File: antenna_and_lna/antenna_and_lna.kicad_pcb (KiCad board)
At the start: 2 copper layers, 9 parts, among them Q1 2SK3557

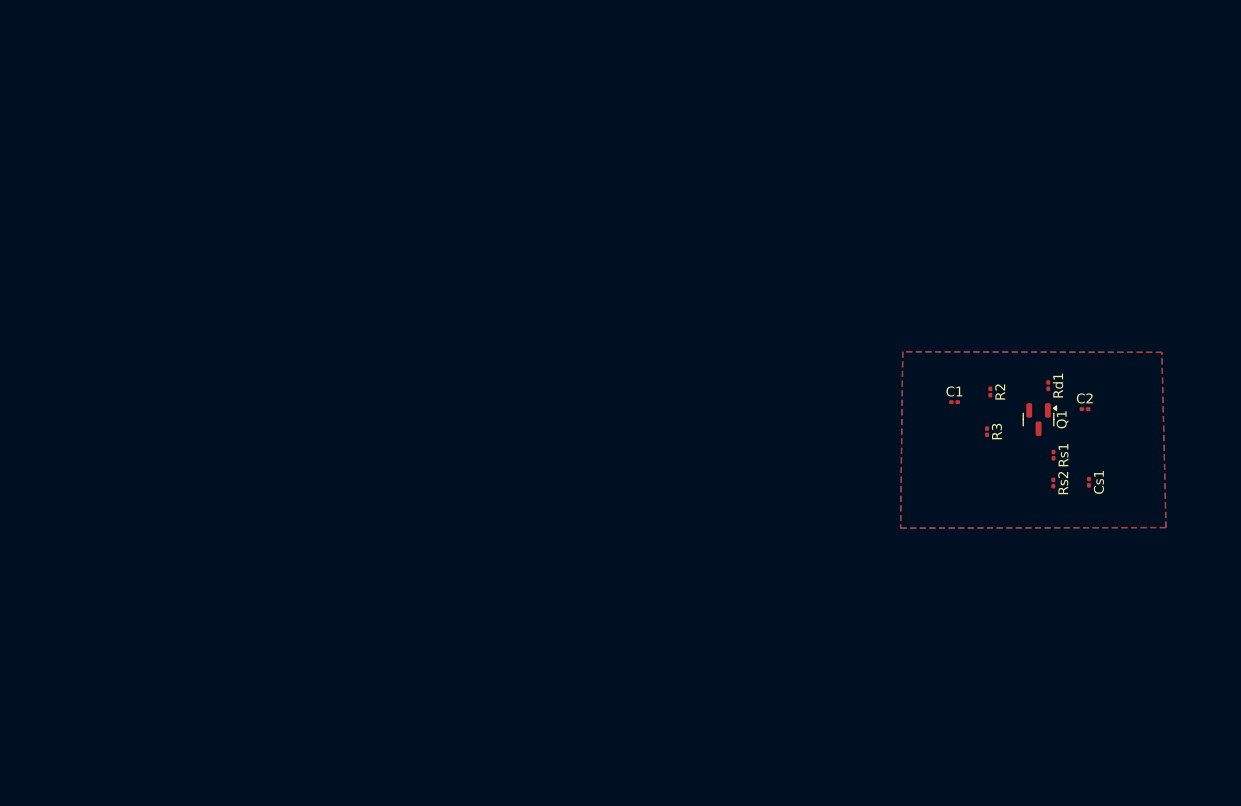
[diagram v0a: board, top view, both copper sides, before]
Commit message: add really rough and imprecise (not to scale at all!) footprints for antenna and tuning cap array
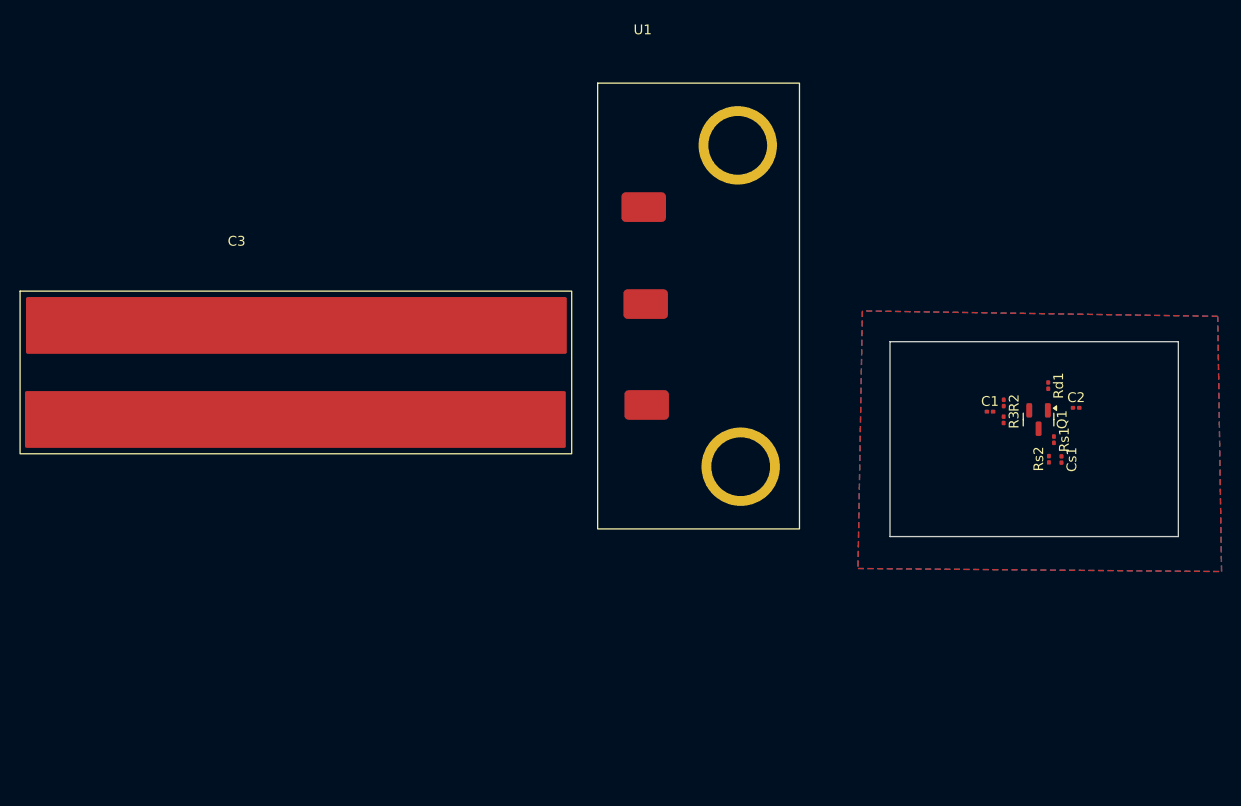
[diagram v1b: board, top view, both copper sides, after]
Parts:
- added C3: C, custom:Tuning_Cap, F.Cu at (77.1, 72.1)
- added U1: ~, custom:Antenna, F.Cu at (118.6, 50.5)
- moved C1 3.74 mm to (154.0, 89.0)
- moved Cs1 3.64 mm to (161.3, 93.9)
- moved Rs2 2.47 mm to (160.1, 93.8)
- moved R3 2.09 mm to (155.4, 89.8)
- moved R2 1.77 mm to (155.4, 88.1)
- moved Rs1 1.58 mm to (160.6, 91.8)
- moved C2 0.92 mm to (162.8, 88.6)
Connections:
- C1 pad 1: unconnected-(C1-Pad1) -> /LNA_in
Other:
- board outline added: 29.4 x 19.9 mm
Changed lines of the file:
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@@
 	(net 2 "Net-(Q1-S)")
 	(net 3 "/LNA/Sigout")
-	(net 4 "unconnected-(C1-Pad1)")
+	(net 4 "/LNA_in")
 	(net 5 "unconnected-(C2-Pad2)")
 	(net 6 "Net-(Cs1-Pad1)")
 	(net 7 "GND")
 	(net 8 "+5V")
+	(net 9 "Net-(U1-Tune)")
 	(footprint "Resistor_SMD:R_0201_0603Metric"
 		(layer "F.Cu")
@@
 	(footprint "Resistor_SMD:R_0201_0603Metric"
 		(layer "F.Cu")
-		(at 154.07 86.975 -90)
+		(at 155.44 88.095 -90)
 		(descr "Resistor SMD 0201 (0603 Metric), square (rectangular) end terminal, IPC-7351 nominal, (Body size source: https://www.vishay.com/docs/20052/crcw0201e3.pdf), generated with kicad-footprint-generator")
 		(tags "resistor")
@@
 	(footprint "Capacitor_SMD:C_0201_0603Metric"
 		(layer "F.Cu")
-		(at 164.14 96.18 -90)
+		(at 161.33 93.865 -90)
 		(descr "Capacitor SMD 0201 (0603 Metric), square (rectangular) end terminal, IPC-7351 nominal, (Body size source: https://www.vishay.com/docs/20052/crcw0201e3.pdf), generated with kicad-footprint-generator")
 		(tags "capacitor")
@@
 	(footprint "Resistor_SMD:R_0201_0603Metric"
 		(layer "F.Cu")
-		(at 160.5 96.27 -90)
+		(at 160.05 93.84 -90)
 		(descr "Resistor SMD 0201 (0603 Metric), square (rectangular) end terminal, IPC-7351 nominal, (Body size source: https://www.vishay.com/docs/20052/crcw0201e3.pdf), generated with kicad-footprint-generator")
 		(tags "resistor")
 		(property "Reference" "Rs2"
-			(at 0 -1.05 90)
+			(at -0.035 1.05 90)
 			(layer "F.SilkS")
 			(effects
@@
 		)
 	)
+	(footprint "custom:Tuning_Cap"
+		(layer "F.Cu")
+		(at 77.14 72.08)
+		(property "Reference" "C3"
+			(at 0 -0.5 0)
+			(unlocked yes)
+			(layer "F.SilkS")
+			(effects
+				(font
+					(size 1 1)
+					(thickness 0.1)
+				)
+			)
+		)
+		(property "Value" "C"
+			(at 0 1 0)
+			(unlocked yes)
+			(layer "F.Fab")
+			(effects
+				(font
+					(size 1 1)
+					(thickness 0.15)
+				)
+			)
+		)
+		(property "Datasheet" "~"
+			(at 0 0 0)
+			(unlocked yes)
+			(layer "F.Fab")
+			(hide yes)
+			(effects
+				(font
+					(size 1 1)
+					(thickness 0.15)
+				)
+			)
+		)
+		(property "Description" "Unpolarized capacitor"
+			(at 0 0 0)
+			(unlocked yes)
+			(layer "F.Fab")
+			(hide yes)
+			(effects
+				(font
+					(size 1 1)
+					(thickness 0.15)
+				)
+			)
+		)
+		(property ki_fp_filters "C_*")
+		(sheetname "/")
+		(sheetfile "antenna_and_lna.kicad_sch")
+		(attr smd)
+		(fp_rect
+			(start -22.1 4.6)
+			(end 34.2 21.2)
+			(stroke
+				(width 0.1)
+				(type default)
+			)
+			(fill no)
+			(layer "F.SilkS")
+		)
+		(fp_text user "${REFERENCE}"
+			(at 0 2.5 0)
+			(unlocked yes)
+			(layer "F.Fab")
+			(effects
+				(font
+					(size 1 1)
+					(thickness 0.15)
+				)
+			)
+		)
+		(pad "1" smd roundrect
+			(at 6.1 8.1)
+			(size 55.2 5.8)
+			(layers "F.Cu" "F.Mask" "F.Paste")
+			(roundrect_rratio 0.03125)
+			(net 7 "GND")
+			(pintype "passive")
+		)
+		(pad "2" smd roundrect
+			(at 6 17.7)
+			(size 55.2 5.8)
+			(layers "F.Cu" "F.Mask" "F.Paste")
+			(roundrect_rratio 0.03125)
+			(net 9 "Net-(U1-Tune)")
+			(pintype "passive")
+		)
+		(embedded_fonts no)
+	)
 	(footprint "Resistor_SMD:R_0201_0603Metric"
 		(layer "F.Cu")
-		(at 160.52 93.42 -90)
+		(at 160.56 91.845 -90)
 		(descr "Resistor SMD 0201 (0603 Metric), square (rectangular) end terminal, IPC-7351 nominal, (Body size source: https://www.vishay.com/docs/20052/crcw0201e3.pdf), generated with kicad-footprint-generator")
 		(tags "resistor")
@@
 	(footprint "Capacitor_SMD:C_0201_0603Metric"
 		(layer "F.Cu")
-		(at 150.425 88.01)
+		(at 154.035 88.98)
 		(descr "Capacitor SMD 0201 (0603 Metric), square (rectangular) end terminal, IPC-7351 nominal, (Body size source: https://www.vishay.com/docs/20052/crcw0201e3.pdf), generated with kicad-footprint-generator")
 		(tags "capacitor")
@@
 			(layers "F.Cu" "F.Mask")
 			(roundrect_rratio 0.25)
-			(net 4 "unconnected-(C1-Pad1)")
+			(net 4 "/LNA_in")
 			(pintype "passive")
 		)
@@
 	(footprint "Capacitor_SMD:C_0201_0603Metric"
 		(layer "F.Cu")
-		(at 163.735 88.72)
+		(at 162.825 88.59)
 		(descr "Capacitor SMD 0201 (0603 Metric), square (rectangular) end terminal, IPC-7351 nominal, (Body size source: https://www.vishay.com/docs/20052/crcw0201e3.pdf), generated with kicad-footprint-generator")
 		(tags "capacitor")
@@
 	(footprint "Resistor_SMD:R_0201_0603Metric"
 		(layer "F.Cu")
-		(at 153.73 91.025 -90)
+		(at 155.43 89.815 -90)
 		(descr "Resistor SMD 0201 (0603 Metric), square (rectangular) end terminal, IPC-7351 nominal, (Body size source: https://www.vishay.com/docs/20052/crcw0201e3.pdf), generated with kicad-footprint-generator")
 		(tags "resistor")
@@
 			)
 		)
+	)
+	(footprint "custom:Antenna"
+		(layer "F.Cu")
+		(at 118.59 50.5)
+		(property "Reference" "U1"
+			(at 0 -0.5 0)
+			(unlocked yes)
+			(layer "F.SilkS")
+			(effects
+				(font
+					(size 1 1)
+					(thickness 0.1)
+				)
+			)
+		)
+		(property "Value" "~"
+			(at 0 1 0)
+			(unlocked yes)
+			(layer "F.Fab")
+			(effects
+				(font
+					(size 1 1)
+					(thickness 0.15)
+				)
+			)
+		)
+		(property "Datasheet" ""
+			(at 0 0 0)
+			(unlocked yes)
+			(layer "F.Fab")
+			(hide yes)
+			(effects
+				(font
+					(size 1 1)
+					(thickness 0.15)
+				)
+			)
+		)
+		(property "Description" ""
+			(at 0 0 0)
+			(unlocked yes)
+			(layer "F.Fab")
+			(hide yes)
+			(effects
+				(font
+					(size 1 1)
+					(thickness 0.15)
+				)
+			)
+		)
+		(sheetname "/")
+		(sheetfile "antenna_and_lna.kicad_sch")
+		(attr smd)
+		(fp_rect
+			(start -4.6 4.95)
+			(end 16 50.45)
+			(stroke
+				(width 0.1)
+				(type default)
+			)
+			(fill no)
+			(layer "F.SilkS")
+		)
+		(fp_text user "${REFERENCE}"
+			(at 0 2.5 0)
+			(unlocked yes)
+			(layer "F.Fab")
+			(effects
+				(font
+					(size 1 1)
+					(thickness 0.15)
+				)
+			)
+		)
+		(pad "" np_thru_hole circle
+			(at 9.7 11.3)
+			(size 8 8)
+			(drill 6)
+			(layers "*.Cu" "*.Mask")
+		)
+		(pad "" np_thru_hole circle
+			(at 10 44.1)
+			(size 8 8)
+			(drill 6)
+			(layers "*.Cu" "*.Mask")
+		)
+		(pad "1" smd roundrect
+			(at 0.1 17.6)
+			(size 4.5525 3.035)
+			(layers "F.Cu" "F.Mask" "F.Paste")
+			(roundrect_rratio 0.15)
+			(net 4 "/LNA_in")
+			(pinfunction "Signal")
+			(pintype "bidirectional")
+		)
+		(pad "2" smd roundrect
+			(at 0.3 27.5)
+			(size 4.5525 3.035)
+			(layers "F.Cu" "F.Mask" "F.Paste")
+			(roundrect_rratio 0.15)
+			(net 7 "GND")
+			(pinfunction "Center_Tap")
+			(pintype "bidirectional")
+		)
+		(pad "3" smd roundrect
+			(at 0.4 37.8)
+			(size 4.5525 3.035)
+			(layers "F.Cu" "F.Mask" "F.Paste")
+			(roundrect_rratio 0.15)
+			(net 9 "Net-(U1-Tune)")
+			(pinfunction "Tune")
+			(pintype "bidirectional")
+		)
+		(embedded_fonts no)
+	)
+	(gr_rect
+		(start 143.83 81.84)
+		(end 173.26 101.73)
+		(stroke
+			(width 0.05)
+			(type default)
+		)
+		(fill no)
+		(layer "Edge.Cuts")
 	)
 	(zone
@@
 		(polygon
 			(pts
-				(xy 145.13 82.87) (xy 144.91 100.87) (xy 172 100.81) (xy 171.58 82.93)
-			)
-		)
+				(xy 141.01 78.7) (xy 140.56 104.99) (xy 177.67 105.3) (xy 177.28 79.25)
+			)
+		)

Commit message: update footprints for antenna and tuning caps
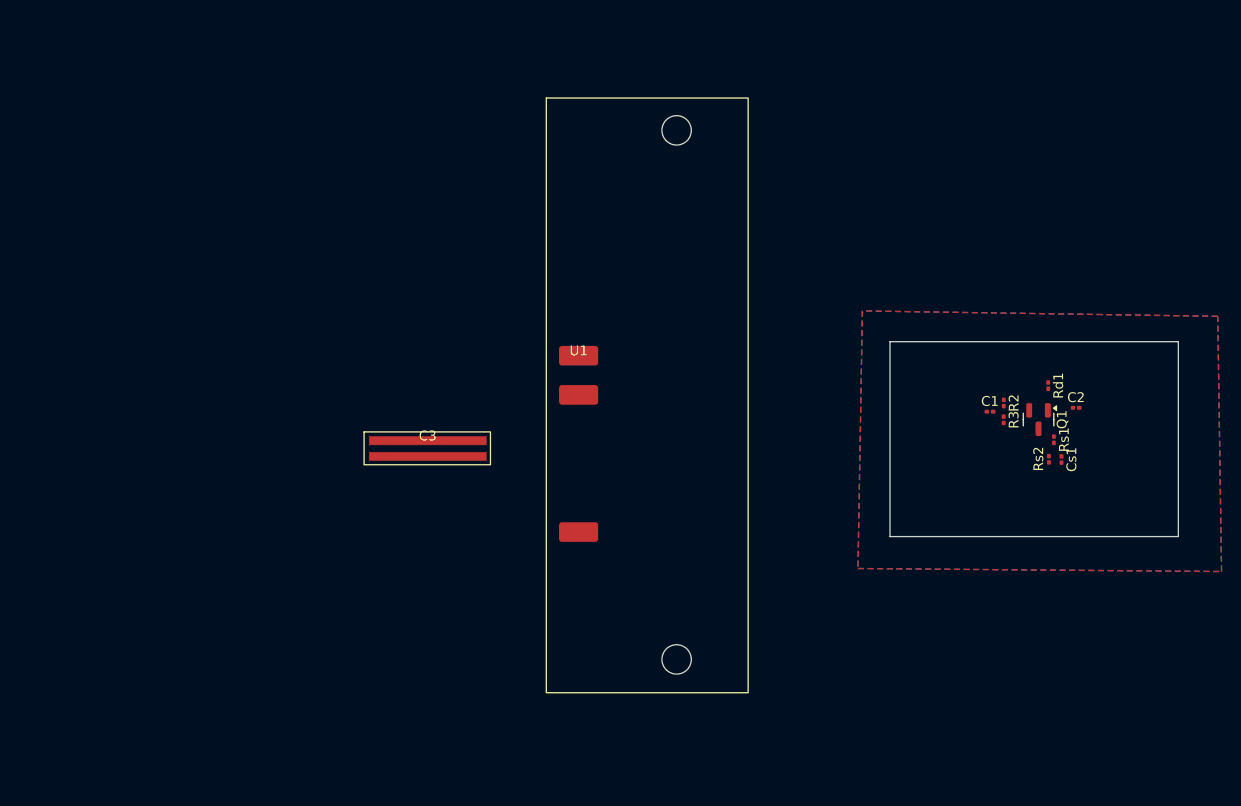
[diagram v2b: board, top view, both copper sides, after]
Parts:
- moved U1 33.4 mm to (112.0, 83.3)
- moved C3 27.8 mm to (96.7, 92.0)
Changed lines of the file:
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@@
 	(footprint "custom:Tuning_Cap"
 		(layer "F.Cu")
-		(at 77.14 72.08)
+		(at 96.65 91.95)
 		(property "Reference" "C3"
 			(at 0 -0.5 0)
@@
 		(attr smd)
 		(fp_rect
-			(start -22.1 4.6)
-			(end 34.2 21.2)
+			(start -6.5 -0.9)
+			(end 6.4 2.45)
 			(stroke
 				(width 0.1)
@@
 		)
 		(pad "1" smd roundrect
-			(at 6.1 8.1)
-			(size 55.2 5.8)
+			(at 0 0)
+			(size 12 0.9)
 			(layers "F.Cu" "F.Mask" "F.Paste")
 			(roundrect_rratio 0.03125)
@@
 		)
 		(pad "2" smd roundrect
-			(at 6 17.7)
-			(size 55.2 5.8)
+			(at 0 1.6)
+			(size 12 0.9)
 			(layers "F.Cu" "F.Mask" "F.Paste")
 			(roundrect_rratio 0.03125)
@@
 	(footprint "custom:Antenna"
 		(layer "F.Cu")
-		(at 118.59 50.5)
+		(at 112.05 83.27)
 		(property "Reference" "U1"
 			(at 0 -0.5 0)
@@
 		(attr smd)
 		(fp_rect
-			(start -4.6 4.95)
-			(end 16 50.45)
+			(start -3.3 -26.3)
+			(end 17.3 34.4)
 			(stroke
 				(width 0.1)
@@
 		)
 		(pad "" np_thru_hole circle
-			(at 9.7 11.3)
-			(size 8 8)
-			(drill 6)
+			(at 10 -23)
+			(size 3 3)
+			(drill 3)
 			(layers "*.Cu" "*.Mask")
 		)
 		(pad "" np_thru_hole circle
-			(at 10 44.1)
-			(size 8 8)
-			(drill 6)
+			(at 10 31)
+			(size 3 3)
+			(drill 3)
 			(layers "*.Cu" "*.Mask")
 		)
 		(pad "1" smd roundrect
-			(at 0.1 17.6)
-			(size 4.5525 3.035)
+			(at 0 0)
+			(size 4 2)
 			(layers "F.Cu" "F.Mask" "F.Paste")
 			(roundrect_rratio 0.15)
@@
 		)
 		(pad "2" smd roundrect
-			(at 0.3 27.5)
-			(size 4.5525 3.035)
+			(at 0 4)
+			(size 4 2)
 			(layers "F.Cu" "F.Mask" "F.Paste")
 			(roundrect_rratio 0.15)
@@
 		)
 		(pad "3" smd roundrect
-			(at 0.4 37.8)
-			(size 4.5525 3.035)
+			(at 0 18)
+			(size 4 2)
 			(layers "F.Cu" "F.Mask" "F.Paste")
 			(roundrect_rratio 0.15)

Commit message: main board gerbers and antenna board layout.
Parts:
- added C4: 10u, Capacitor_SMD:C_0603_1608Metric, F.Cu at (107.5, 83.3)
- added C5: 100n, Capacitor_SMD:C_0603_1608Metric, F.Cu at (98.7, 80.5)
- added C6: 3.3n, Capacitor_SMD:C_0603_1608Metric, F.Cu at (105.2, 104.4)
- added J1: CON-SMA-EDGE-S, SMA_fp:RFSOLUTIONS_CON-SMA-EDGE-S, F.Cu at (110.0, 124.3)
- added J2: TSW-104-14-F-S, pin_header_fp:CON4_1X4_TU_TSW, F.Cu at (112.5, 86.5)
- added L1: 27 u, Inductor_SMD:L_0603_1608Metric, F.Cu at (109.8, 117.6)
- C1: value C -> 100n; footprint Capacitor_SMD:C_0201_0603Metric -> Capacitor_SMD:C_0603_1608Metric
- C2: value C -> .012u; footprint Capacitor_SMD:C_0201_0603Metric -> Capacitor_SMD:C_0603_1608Metric
- Cs1: footprint Capacitor_SMD:C_0201_0603Metric -> Capacitor_SMD:C_0603_1608Metric
- R2, R3, Rd1, Rs1, Rs2: footprint Resistor_SMD:R_0201_0603Metric -> Resistor_SMD:R_0603_1608Metric
- moved Cs1 64.5 mm to (96.8, 94.4)
- moved C1 61.0 mm to (93.1, 86.2)
- moved R2 58.6 mm to (97.0, 83.9)
- moved Rs1 58.6 mm to (102.0, 92.3)
- moved R3 58.5 mm to (96.9, 89.0)
- moved Rs2 58.1 mm to (102.0, 95.9)
- moved Rd1 57.9 mm to (102.2, 83.3)
- moved Q1 57.0 mm to (102.0, 87.6)
- moved C2 54.8 mm to (108.0, 89.0), turned to -90 degrees
- moved U1 33.0 mm to (79.1, 85.0)
- moved C3 15.5 mm to (88.9, 105.4), turned to 90 degrees
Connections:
- C2 pad 2: unconnected-(C2-Pad2) -> Net-(C2-Pad2)
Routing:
- net GND: track 0.00 -> 61.1 mm, vias 0 -> 5
- net Net-(C2-Pad2): track 0.00 -> 27.8 mm
- net +5V: track 0.00 -> 26.0 mm
- net /LNA/Sigout: track 0.00 -> 24.3 mm
- net /ant_to_main: track 0.00 -> 20.7 mm
- net Net-(U1-Tune): track 0.00 -> 20.0 mm
- net /LNA_in: track 0.00 -> 13.5 mm
- net /LNA/Sigin: track 0.00 -> 11.2 mm
- net Net-(Cs1-Pad1): track 0.00 -> 7.37 mm
- net Net-(Q1-S): track 0.00 -> 2.94 mm
- removed copper zone on F.Cu, net GND
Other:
- board size 29.4 x 19.9 mm -> 40 x 70 mm
